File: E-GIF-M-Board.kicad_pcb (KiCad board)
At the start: 2 copper layers, 100 x 100 mm, 109 parts, among them CON1 PWR_JACK, CON2 Micro_SD_Card, IC1 MAX3232, J2 RJ45-TRANSFO, J3 RJ45-TRANSFO, J4 MDB9_IN, J5 MDB9_OUT, P4 DEBUG, P6 TB_IN, P7 TB_OUT, U1 MCP16312-E/MS, U2 ARIA-G25, U3 MCP2200, U4 LAN9500A, U5 ST3485EBDR, U6 ST3485EBDR, Y1 16MHz, Y2 25MHz

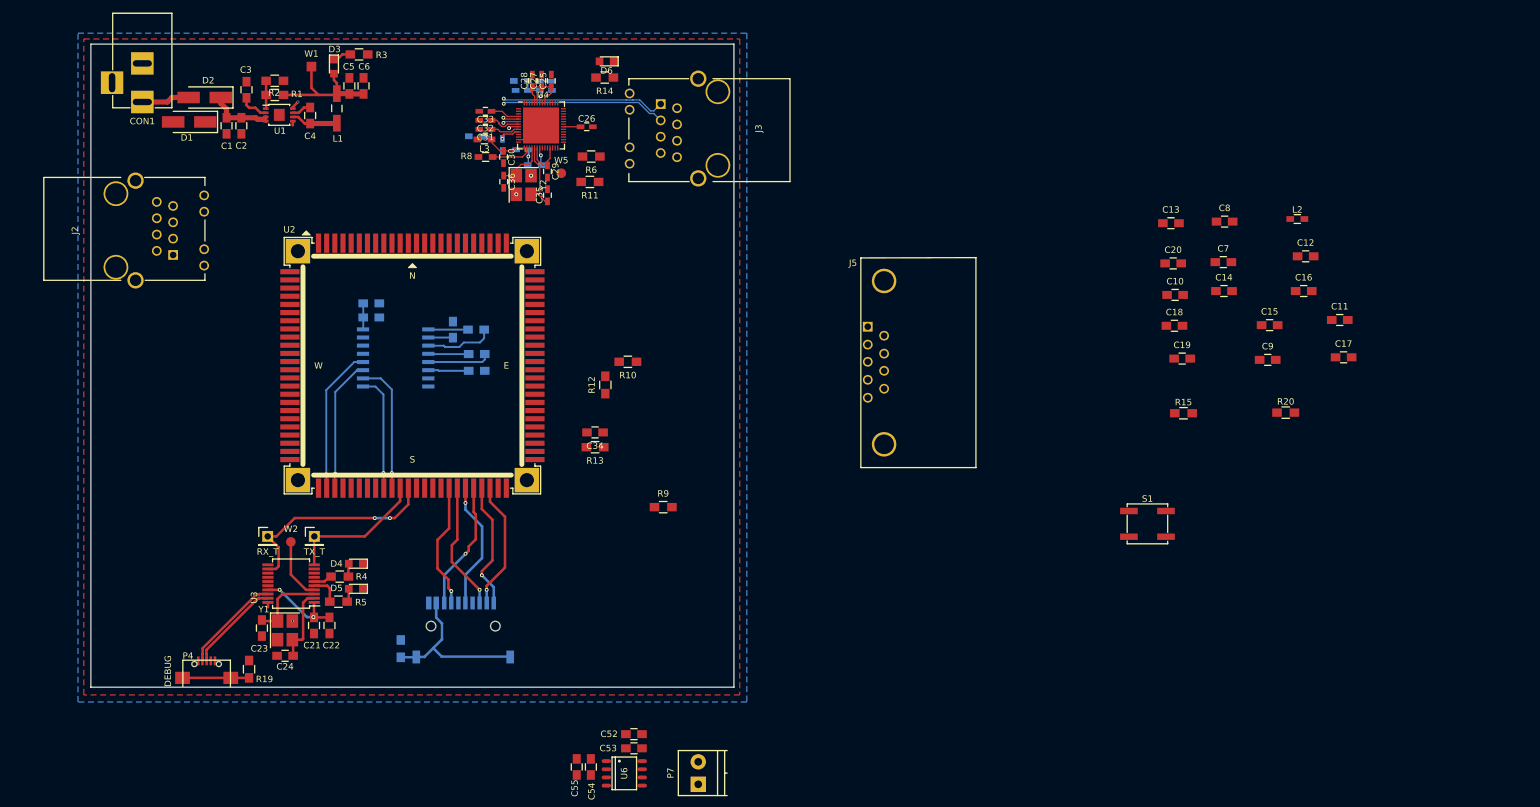
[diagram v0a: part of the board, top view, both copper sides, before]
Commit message: Modified USB/ETH label names.
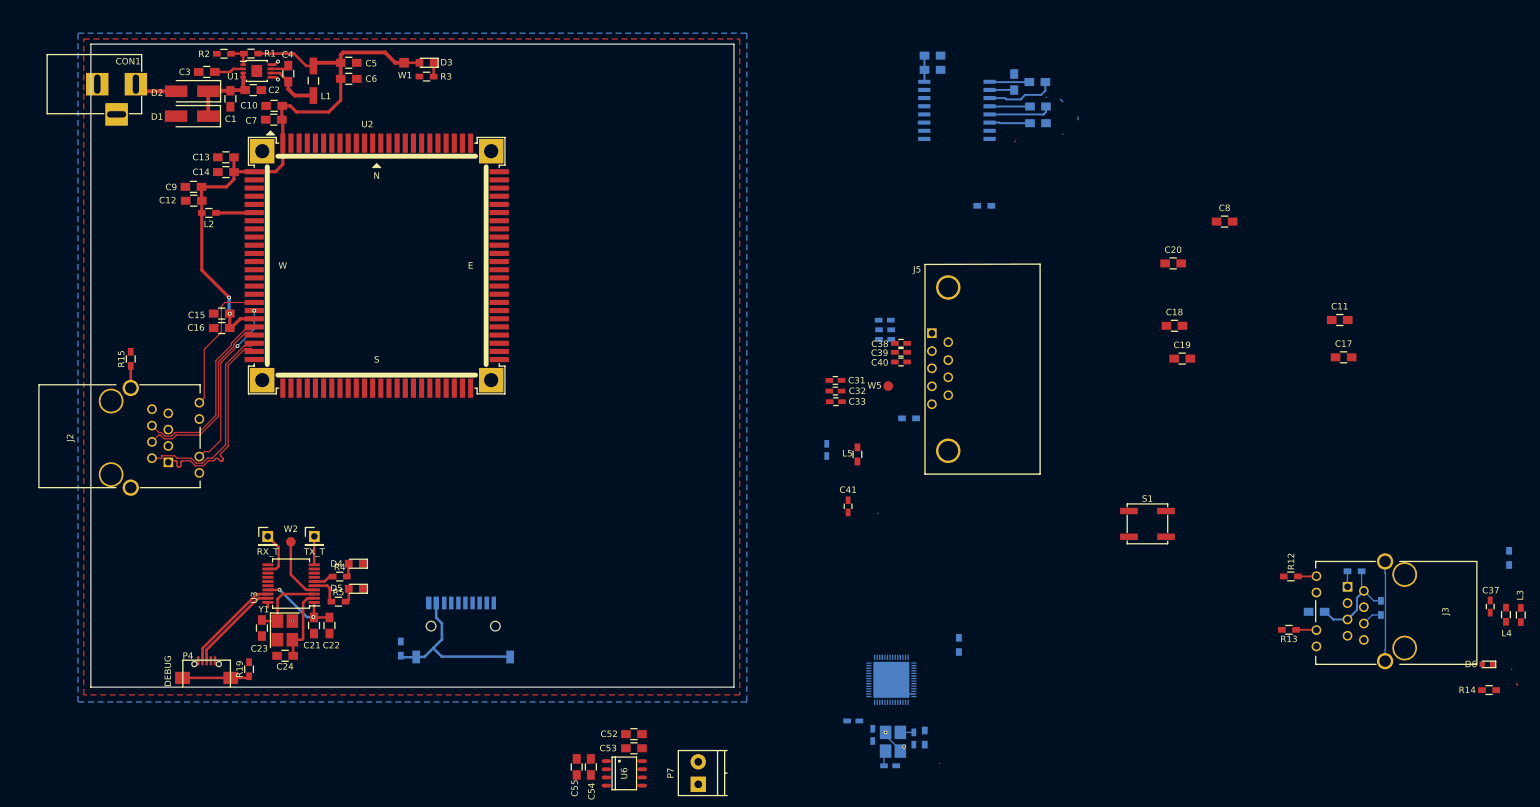
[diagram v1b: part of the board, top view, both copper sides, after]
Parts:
- C25, C26, C27, C28, C29, C30, C34, C35, C36, R8, U4, Y2: moved to B.Cu
- C37, C38, C39, C40, C41, L4, L5: moved to F.Cu
- D6: footprint LEDs:LED_0805 -> LEDs:LED_0603
- R1, R12, R13, R14, R15, R16, R19, R2, R3, R4, R5: footprint Resistors_SMD:R_0805_HandSoldering -> Resistors_SMD:R_0603_HandSoldering
- R10, R11, R20, R6, R9: footprint Resistors_SMD:R_0805_HandSoldering -> Resistors_SMD:R_0603_HandSoldering; moved to B.Cu
- moved L3 177.3 mm to (242.3, 108.8), turned to 270 degrees
- moved C12 173.1 mm to (36.0, 44.4), turned to 180 degrees
- moved L2 169.3 mm to (38.4, 46.2)
- moved C9 169.2 mm to (36.0, 42.2), turned to 180 degrees
- moved C16 168.3 mm to (40.4, 64.2), turned to 180 degrees
- moved R14 167.3 mm to (237.4, 120.5), turned to 0 degrees
- moved C37 166.4 mm to (237.6, 107.5), turned to 90 degrees
- moved L4 166.4 mm to (240.1, 108.7), turned to 270 degrees
- moved D6 166.0 mm to (237.2, 116.5)
- moved R15 163.9 mm to (26.2, 69.0), turned to 90 degrees
- moved C15 163.0 mm to (40.4, 61.9), turned to 180 degrees
- moved C14 156.3 mm to (41.0, 39.9), turned to 180 degrees
- moved R6 155.8 mm to (240.5, 99.9), turned to 270 degrees
- moved C7 149.3 mm to (48.5, 31.8), turned to 180 degrees
- moved C13 147.3 mm to (41.0, 37.6), turned to 180 degrees
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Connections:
- net /AriaG25Module/ETHRXN renamed /AriaG25Module/ETHRX_N
- net /AriaG25Module/ETHRXP renamed /AriaG25Module/ETHRX_P
- net /AriaG25Module/ETHTXN renamed /AriaG25Module/ETHTX_N
- net /AriaG25Module/ETHTXP renamed /AriaG25Module/ETHTX_P
- net /AriaG25Module/USBAN renamed /AriaG25Module/USBA_N
- net /AriaG25Module/USBAP renamed /AriaG25Module/USBA_P
- net /AriaG25Module/USBBN renamed /AriaG25Module/USBB_N
- net /AriaG25Module/USBBP renamed /AriaG25Module/USBB_P
- net /AriaG25Module/USBCN renamed /AriaG25Module/USBC_N
- net /AriaG25Module/USBCP renamed /AriaG25Module/USBC_P
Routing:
- net +3V3: track 60.3 -> 116.5 mm, vias 2 -> 4
- net /AriaG25Module/ETHRX_P: track 0.00 -> 31.8 mm
- net /AriaG25Module/ETHRX_N: track 0.00 -> 31.8 mm
- net /AriaG25Module/ETHTX_P: track 0.00 -> 28.8 mm
- net /AriaG25Module/ETHTX_N: track 0.00 -> 28.8 mm
- net /AriaG25Module/ETHLED1: track 0.00 -> 26.7 mm, vias 0 -> 2
- net /AriaG25Module/DTXD: track 33.7 -> 7.20 mm, vias 2 -> 0
- net /Interfaces/USB_ETH_conv/TX-: track 25.7 -> 0.40 mm, vias 1 -> 0
- net /Interfaces/RS232_IN_RX: track 22.8 -> 0.00 mm, vias 1 -> 0
- net /Interfaces/USB_ETH_conv/TX+: track 25.7 -> 2.98 mm, vias 1 -> 0
- net /AriaG25Module/ETHLED2: track 0.00 -> 21.8 mm
- net /Interfaces/RS232_OUT_TX: track 20.6 -> 0.00 mm, vias 1 -> 0
- net /AriaG25Module/DA1: track 20.0 -> 0.00 mm, vias 1 -> 0
- net /AriaG25Module/DA3: track 20.0 -> 0.05 mm, vias 1 -> 0
- net /AriaG25Module/CDA: track 20.0 -> 0.00 mm, vias 1 -> 0
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
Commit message: Finished first version of PCB.
Modified RJ45 footprint.
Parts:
- removed J2, J3: RJ45-TRANSFO, Connectors:RJ45_TRANSFO
- added CON3: RJ45-TRF-LED, misc:RJ45_TRANSFO, F.Cu at (36.0, 80.1)
- added CON4: RJ45-TRF-LED, misc:RJ45_TRANSFO, F.Cu at (104.0, 81.7)
- added R17: R, Resistors_SMD:R_0805_HandSoldering, F.Cu at (65.7, 97.9)
- BT1, C33: moved to B.Cu
- C1, C2: footprint Capacitors_SMD:C_0805_HandSoldering -> Capacitors_SMD:CP_Elec_5x4.5
- C28, C30, R20, R6: moved to F.Cu
- S1: footprint Buttons_Switches_SMD:SW_SPST_EVPBF -> misc:SW_SPST_EVPBF
- moved BT1 159.2 mm to (98.4, 114.7)
- moved R14 155.8 mm to (96.4, 54.3), turned to 270 degrees
- moved D6 155.8 mm to (94.5, 53.9), turned to 270 degrees
- moved L3 155.6 mm to (92.7, 66.1), turned to 180 degrees
- moved L4 153.0 mm to (93.9, 63.5), turned to 90 degrees
- moved C37 152.7 mm to (91.1, 64.5), turned to 180 degrees
- moved C11 152.4 mm to (63.0, 82.2)
- moved R6 143.6 mm to (99.5, 72.9)
- moved C8 138.3 mm to (63.0, 84.5)
- moved C17 135.0 mm to (80.1, 78.4)
- moved R9 124.6 mm to (99.3, 79.0), turned to 0 degrees
- moved S1 120.7 mm to (63.7, 90.6), turned to 90 degrees
- moved R10 119.0 mm to (98.6, 86.1), turned to 0 degrees
- moved C20 116.6 mm to (81.2, 100.2)
- moved C34 115.5 mm to (98.1, 82.3)
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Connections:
- C11 pad 1: +3V3 -> /AriaG25Module/~RST
- C8 pad 1: +3V3 -> /AriaG25Module/~RST
- R12 pad 1: Net-(J3-PadGK) -> /Interfaces/USB_ETH_conv/nLNKA_LED
- R12 pad 2: Net-(R12-Pad2) -> Net-(CON4-Pad10)
- R13 pad 1: Net-(J3-PadYK) -> /Interfaces/USB_ETH_conv/nSPD_LED
- R13 pad 2: Net-(R13-Pad2) -> Net-(CON4-Pad12)
- S1 pad 1: +3V3 -> /AriaG25Module/~RST
- S1 pad 2: +3V3 -> /AriaG25Module/~RST
- U2 pad E2: /Interfaces/RS485_OUT_DI -> /Interfaces/RS232_OUT_RX
- U2 pad E21: +3V3 -> /AriaG25Module/~RST
- U2 pad E3: /Interfaces/RS485_OUT_RO -> /Interfaces/RS232_OUT_TX
- U2 pad S15: /Interfaces/RS232_OUT_TX -> /Interfaces/RS485_OUT_RO
- U2 pad S16: /Interfaces/RS232_OUT_RX -> /Interfaces/RS485_OUT_DI
- U4 pad 27: Net-(R12-Pad2) -> /Interfaces/USB_ETH_conv/nLNKA_LED
- U4 pad 28: Net-(R13-Pad2) -> /Interfaces/USB_ETH_conv/nSPD_LED
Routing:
- net +3V3: track 116.5 -> 479.0 mm, vias 4 -> 13
- net /VBUS: track 0.00 -> 100.9 mm
- net /AriaG25Module/VBAT: track 0.00 -> 71.6 mm, vias 0 -> 2
- net /Interfaces/RS485_OUT_DI: track 0.00 -> 66.4 mm, vias 0 -> 2
- net /Interfaces/RS485_OUT_RO: track 0.00 -> 60.9 mm
- net /Interfaces/SERIAL_RS232_conv/R2: track 0.00 -> 52.4 mm, vias 0 -> 1
- net /AriaG25Module/~RST: track 0.00 -> 52.4 mm, vias 0 -> 2
- net /Interfaces/SERIAL_RS232_conv/T2: track 0.00 -> 51.7 mm, vias 0 -> 1
- net /AriaG25Module/CDA: track 0.00 -> 39.9 mm, vias 0 -> 3
- net /AriaG25Module/DA2: track 0.00 -> 36.7 mm, vias 0 -> 1
- net /Interfaces/RS232_OUT_RX: track 0.00 -> 36.0 mm, vias 0 -> 1
- net /AriaG25Module/DTXD: track 7.20 -> 43.0 mm, vias 0 -> 1
- net /Interfaces/RS485_IN_RO: track 0.00 -> 35.7 mm
- net /AriaG25Module/DA1: track 0.00 -> 35.6 mm, vias 0 -> 1
- net /Interfaces/USB_ETH_conv/TX+: track 2.98 -> 37.6 mm, vias 0 -> 1
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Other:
- rule via_min_size: 0.4 -> 0.6

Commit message: Modified buck circuit on board.
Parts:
- added R18: 1M, Resistors_SMD:R_0603_HandSoldering, B.Cu at (61.5, 25.9)
- C1, C2: footprint Capacitors_SMD:CP_Elec_5x4.5 -> Capacitors_SMD:C_0603_HandSoldering; moved to B.Cu
- C10, C11, C12, C13, C14, C15, C16, C17, C18, C19, C20, C21, C22, C23, C24, C42, C43, C44, C45, C46, C47, C48, C49, C50, C51, C52, C53, C54, C55, C7, C8, C9: footprint Capacitors_SMD:C_0805_HandSoldering -> Capacitors_SMD:C_0603_HandSoldering
- C3, C4, C5, C6: footprint Capacitors_SMD:C_0805_HandSoldering -> Capacitors_SMD:C_0603_HandSoldering; moved to B.Cu
- C34: value 22nF -> .022uF; footprint Capacitors_SMD:C_0805_HandSoldering -> Capacitors_SMD:C_0603_HandSoldering
- D1, D2, R1, R2, U1: moved to B.Cu
- D3, D4, D5: footprint LEDs:LED_0805 -> LEDs:LED_0603
- L1: footprint Choke_SMD:Choke_SMD_1206_Handsoldering -> Inductors:Inductor_Taiyo-Yuden_MD-5050; moved to B.Cu
- R17: value R -> 1k; footprint Resistors_SMD:R_0805_HandSoldering -> Resistors_SMD:R_0603_HandSoldering
- R3, R4, R5: value R -> 220
- moved C2 32.8 mm to (67.0, 23.2), turned to 0 degrees
- moved R2 27.5 mm to (67.1, 29.1), turned to 0 degrees
- moved C6 24.1 mm to (84.2, 27.3), turned to 90 degrees
- moved R1 24.0 mm to (67.1, 30.7)
- moved R3 23.7 mm to (48.5, 24.4)
- moved C3 23.6 mm to (61.5, 27.4)
- moved C1 23.0 mm to (67.0, 21.9)
- moved C5 22.7 mm to (82.3, 27.3), turned to 90 degrees
- moved U1 22.5 mm to (68.2, 26.3)
- moved L1 22.5 mm to (77.1, 26.4), turned to 90 degrees
- moved C4 22.1 mm to (72.7, 26.4), turned to 270 degrees
- moved D3 20.1 mm to (52.1, 24.4), turned to 0 degrees
- moved D2 15.0 mm to (50.5, 24.5)
- moved D1 15.0 mm to (50.5, 28.8)
- moved CON1 11.6 mm to (39.1, 29.9)
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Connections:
- U1 pad 3: /Power/VIN -> Net-(R18-Pad1)
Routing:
- net +3V3: track 479.0 -> 458.9 mm, vias 13 -> 15
- net /VBUS: track 100.9 -> 116.6 mm, vias 0 -> 1
- net /Power/VIN: track 19.7 -> 26.7 mm
- net /Power/VFB: track 5.11 -> 0.00 mm
- net Net-(CON1-Pad1): track 7.44 -> 11.1 mm
- net Net-(R18-Pad1): track 0.00 -> 3.54 mm
- net GND: track 14.4 -> 13.2 mm, vias 14 -> 13
- net Net-(C4-Pad1): track 8.22 -> 7.32 mm
- net Net-(C3-Pad1): track 4.62 -> 4.07 mm

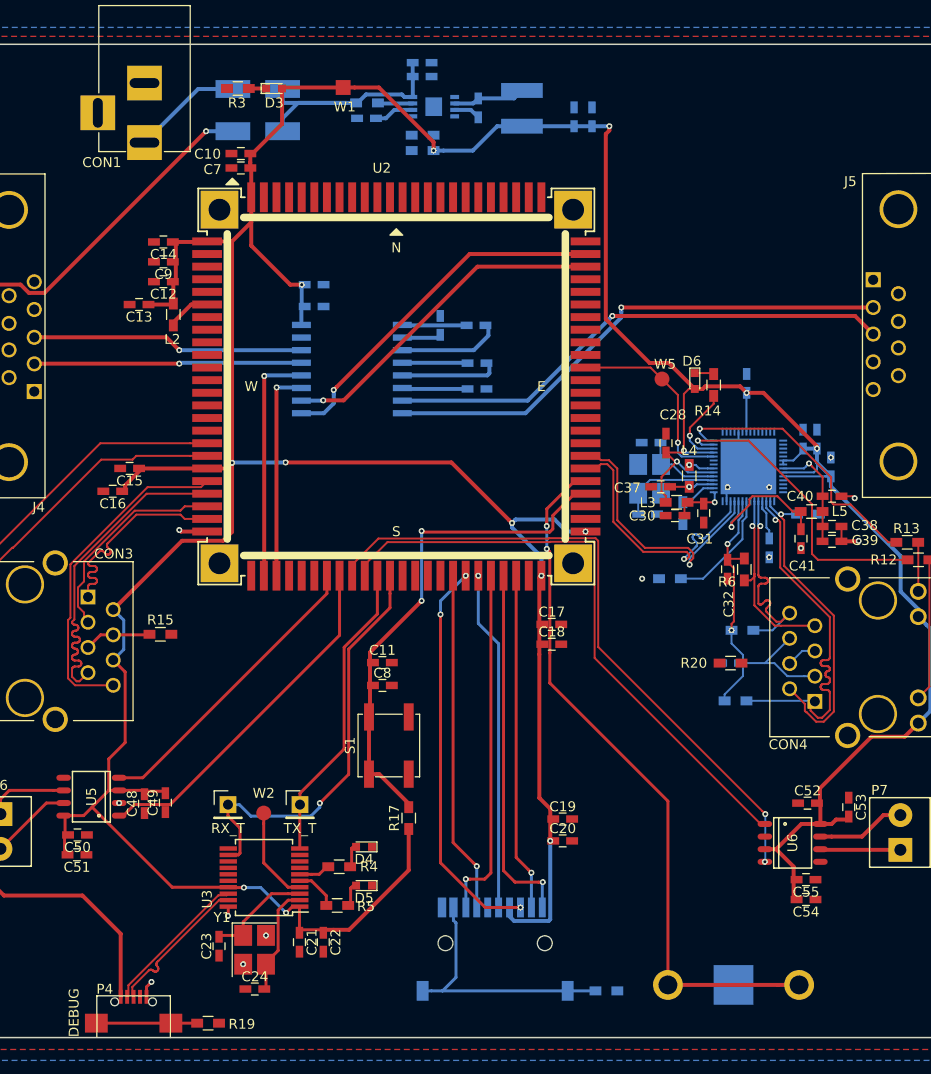
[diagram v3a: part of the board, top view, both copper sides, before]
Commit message: Removed some capacitors.
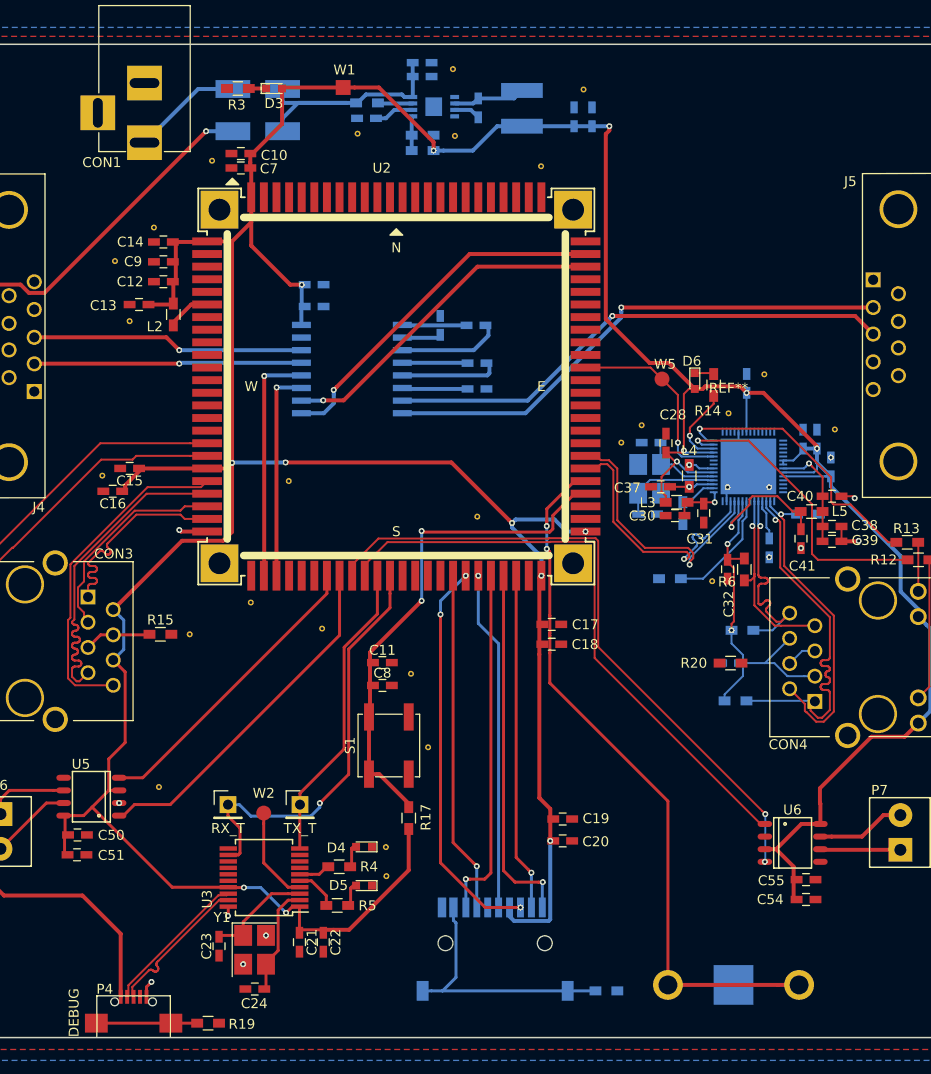
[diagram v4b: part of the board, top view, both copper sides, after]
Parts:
- removed C48, C52: 100nF, Capacitors_SMD:C_0603_HandSoldering
- removed C49, C53: 1uF, Capacitors_SMD:C_0603_HandSoldering
- added REF**: SolderWirePad_single_0-8mmDrill, Wire_Pads:SolderWirePad_single_0-8mmDrill, F.Cu at (96.2, 74.0)
- added REF**: SolderWirePad_single_0-8mmDrill, Wire_Pads:SolderWirePad_single_0-8mmDrill, F.Cu at (63.4, 100.8)
- added REF**: SolderWirePad_single_0-8mmDrill, Wire_Pads:SolderWirePad_single_0-8mmDrill, F.Cu at (67.7, 90.8)
- added REF**: SolderWirePad_single_0-8mmDrill, Wire_Pads:SolderWirePad_single_0-8mmDrill, F.Cu at (65.9, 83.4)
- added REF**: SolderWirePad_single_0-8mmDrill, Wire_Pads:SolderWirePad_single_0-8mmDrill, F.Cu at (49.8, 76.2)
- added REF**: SolderWirePad_single_0-8mmDrill, Wire_Pads:SolderWirePad_single_0-8mmDrill, F.Cu at (43.6, 79.4)
- added REF**: SolderWirePad_single_0-8mmDrill, Wire_Pads:SolderWirePad_single_0-8mmDrill, F.Cu at (34.9, 63.4)
- added REF**: SolderWirePad_single_0-8mmDrill, Wire_Pads:SolderWirePad_single_0-8mmDrill, F.Cu at (37.6, 47.9)
- added REF**: SolderWirePad_single_0-8mmDrill, Wire_Pads:SolderWirePad_single_0-8mmDrill, F.Cu at (36.1, 41.8)
- added REF**: SolderWirePad_single_0-8mmDrill, Wire_Pads:SolderWirePad_single_0-8mmDrill, F.Cu at (40.0, 38.5)
- added REF**: SolderWirePad_single_0-8mmDrill, Wire_Pads:SolderWirePad_single_0-8mmDrill, F.Cu at (45.9, 31.7)
- added REF**: SolderWirePad_single_0-8mmDrill, Wire_Pads:SolderWirePad_single_0-8mmDrill, F.Cu at (108.6, 58.8)
- added REF**: SolderWirePad_single_0-8mmDrill, Wire_Pads:SolderWirePad_single_0-8mmDrill, F.Cu at (83.3, 24.6)
- added REF**: SolderWirePad_single_0-8mmDrill, Wire_Pads:SolderWirePad_single_0-8mmDrill, F.Cu at (70.3, 29.2)
- added REF**: SolderWirePad_single_0-8mmDrill, Wire_Pads:SolderWirePad_single_0-8mmDrill, F.Cu at (70.2, 22.5)
- added REF**: SolderWirePad_single_0-8mmDrill, Wire_Pads:SolderWirePad_single_0-8mmDrill, F.Cu at (60.5, 29.0)
- added REF**: SolderWirePad_single_0-8mmDrill, Wire_Pads:SolderWirePad_single_0-8mmDrill, F.Cu at (87.1, 60.1)
- added REF**: SolderWirePad_single_0-8mmDrill, Wire_Pads:SolderWirePad_single_0-8mmDrill, F.Cu at (89.2, 58.4)
- added REF**: SolderWirePad_single_0-8mmDrill, Wire_Pads:SolderWirePad_single_0-8mmDrill, F.Cu at (97.9, 57.1)
- added REF**: SolderWirePad_single_0-8mmDrill, Wire_Pads:SolderWirePad_single_0-8mmDrill, F.Cu at (101.5, 53.2)
- added REF**: SolderWirePad_single_0-8mmDrill, Wire_Pads:SolderWirePad_single_0-8mmDrill, F.Cu at (40.5, 94.8)
- added REF**: SolderWirePad_single_0-8mmDrill, Wire_Pads:SolderWirePad_single_0-8mmDrill, F.Cu at (57.0, 78.8)
- added REF**: SolderWirePad_single_0-8mmDrill, Wire_Pads:SolderWirePad_single_0-8mmDrill, F.Cu at (72.6, 67.5)
- added REF**: SolderWirePad_single_0-8mmDrill, Wire_Pads:SolderWirePad_single_0-8mmDrill, F.Cu at (53.6, 64.0)
- added REF**: SolderWirePad_single_0-8mmDrill, Wire_Pads:SolderWirePad_single_0-8mmDrill, F.Cu at (79.0, 32.3)
- added REF**: SolderWirePad_single_0-8mmDrill, Wire_Pads:SolderWirePad_single_0-8mmDrill, F.Cu at (63.5, 103.8)
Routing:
- net +3V3: track 458.9 -> 451.1 mm
- net /Power/VFB: track 0.00 -> 3.49 mm
- net (no net): vias 1 -> 0
